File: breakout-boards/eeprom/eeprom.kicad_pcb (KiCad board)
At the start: 2 copper layers, 24.1 x 10.8 mm, 8 parts, among them J1 BREAKOUT, U1 AP2127N-3.3, U2 M95256-WMN6P

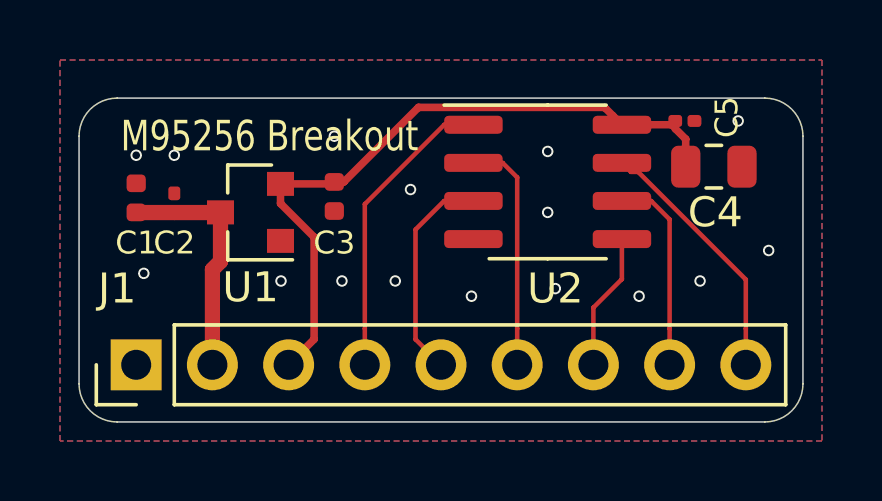
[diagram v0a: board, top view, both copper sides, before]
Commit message: (#14) redo stm32 and eeprom board to only include 0603 and 0805 components
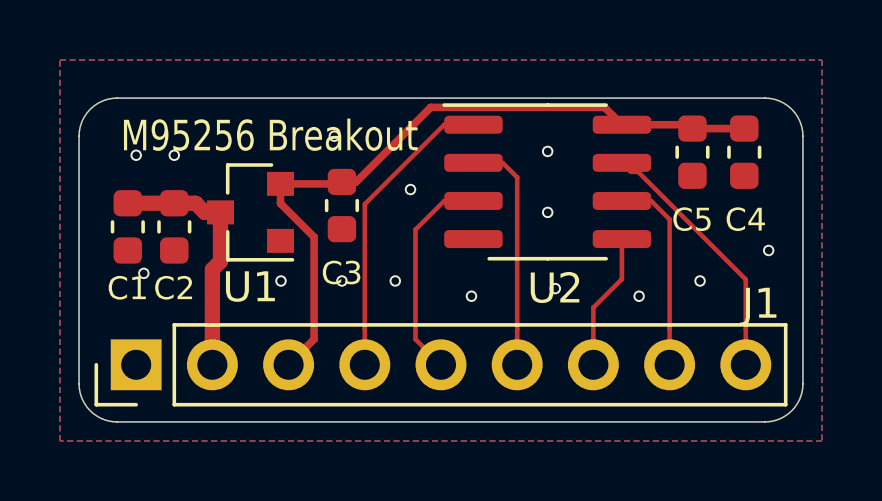
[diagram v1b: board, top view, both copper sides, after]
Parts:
- C1, C3: footprint Capacitor_SMD:C_0402_1005Metric -> Capacitor_SMD:C_0603_1608Metric
- C2, C5: footprint Capacitor_SMD:C_0201_0603Metric -> Capacitor_SMD:C_0603_1608Metric
- C4: footprint Capacitor_SMD:C_0805_2012Metric -> Capacitor_SMD:C_0603_1608Metric
- moved C4 1.12 mm to (147.3, 94.5), turned to 270 degrees
- moved C5 1.07 mm to (145.5, 94.5), turned to 270 degrees
- moved C1 1.01 mm to (126.7, 97.0), turned to 270 degrees
- moved C2 0.80 mm to (128.3, 97.0), turned to 270 degrees
- moved C3 0.39 mm to (133.9, 96.3)
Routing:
- net +3V3: track 23.0 -> 23.7 mm
- net GND: vias 16 -> 15
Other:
- board text added: "M95256 Breakout Board | Rev. B The UltraBoard Project Wesley Soo-Hoo | 1/6/2020"
- board text removed: "M95256 Breakout Board The UltraBoard Project Wesley Soo-Hoo | 1/6/2020"
